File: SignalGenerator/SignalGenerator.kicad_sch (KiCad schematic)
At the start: 36 parts, among them J1 Buss PD, J2 AVR-ICSP, J3 I2C Display, J4 Conn_Coaxial, J5 Screw_Terminal_01x04, J6 Power, SW1 SW_Push_SPDT, U2 ATmega328-A, U5 AD8021, U6 AD9833BRMZ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

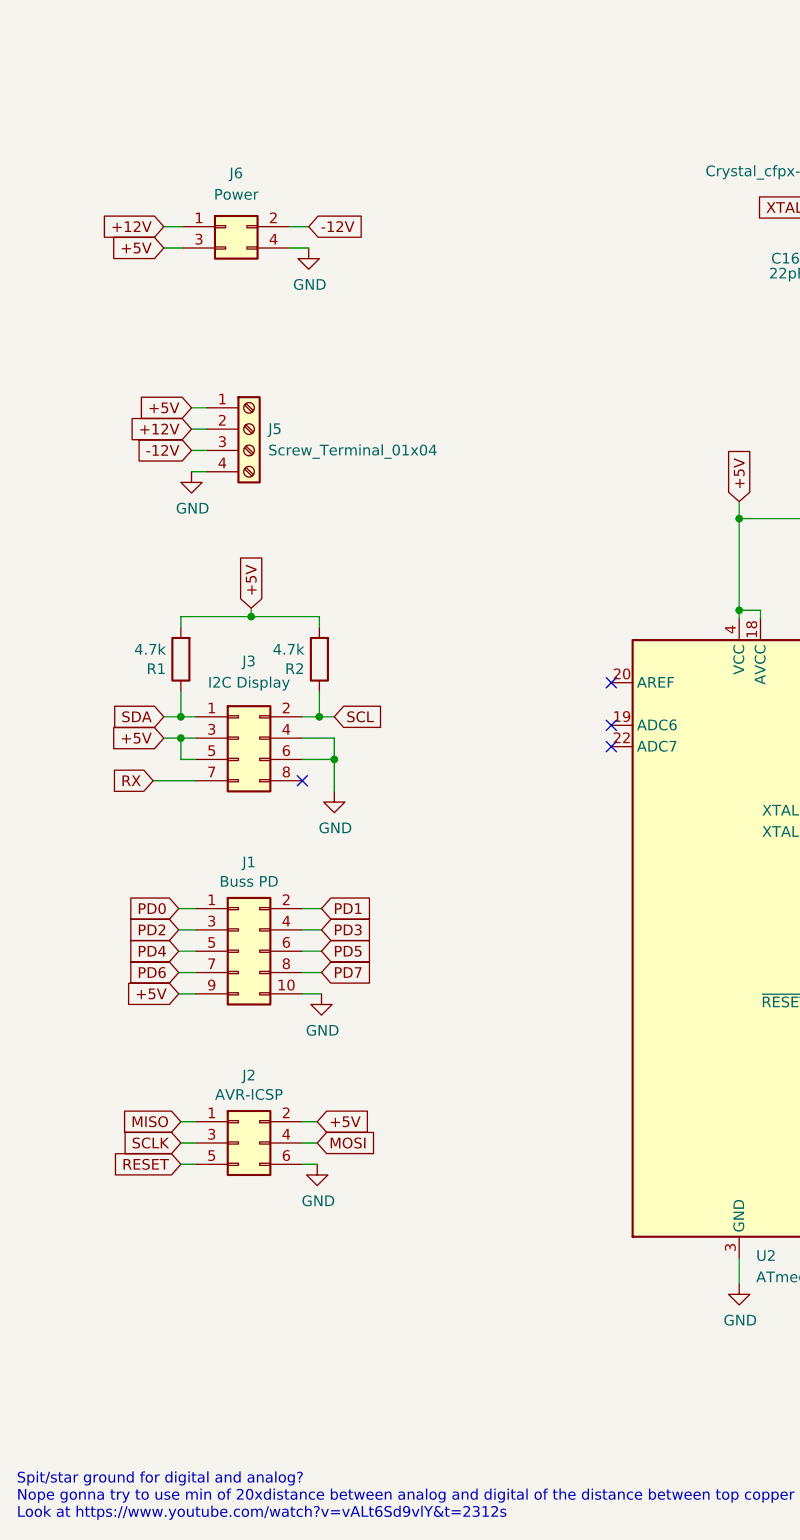
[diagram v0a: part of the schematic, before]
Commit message: added rotary encoder stuff
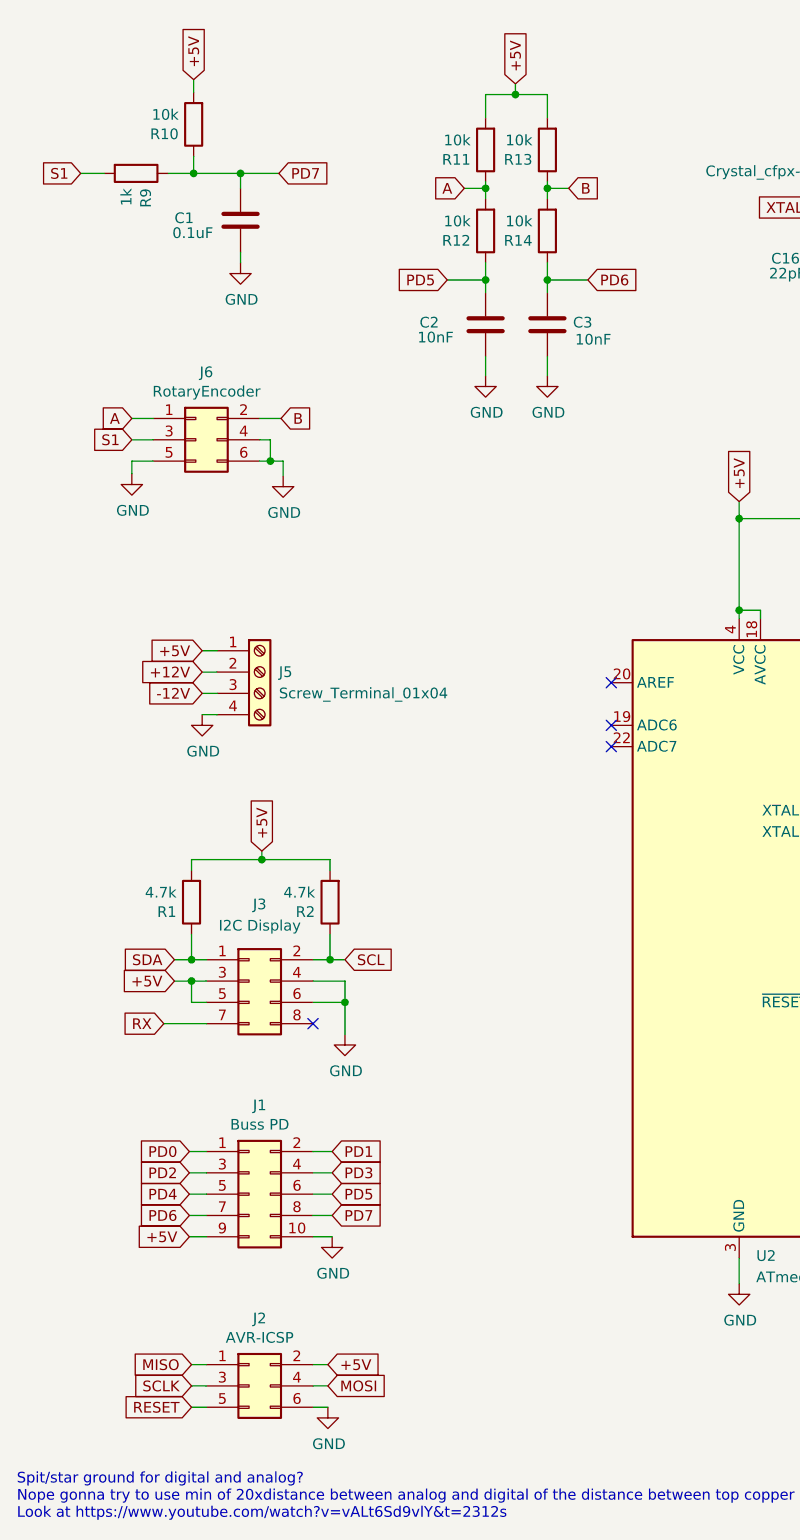
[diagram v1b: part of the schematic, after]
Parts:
- removed J6: Power, Connector_PinHeader_2.54mm:PinHeader_2x02_P2.54mm_Vertical, symbol Connector_Generic:Conn_02x02_Odd_Even
- added C1: 0.1uF, Capacitor_SMD:C_0805_2012Metric_Pad1.18x1.45mm_HandSolder, symbol Device:C
- added C2, C3: 10nF, Capacitor_SMD:C_1206_3216Metric_Pad1.33x1.80mm_HandSolder, symbol Device:C
- added J6: RotaryEncoder, Connector_PinHeader_2.54mm:PinHeader_2x03_P2.54mm_Vertical, symbol Connector_Generic:Conn_02x03_Odd_Even
- added R10, R11, R12, R13, R14: 10k, Resistor_SMD:R_0805_2012Metric_Pad1.20x1.40mm_HandSolder, symbol Device:R
- added R9: 1k, Resistor_SMD:R_0805_2012Metric_Pad1.20x1.40mm_HandSolder, symbol Device:R
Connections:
- net +5V: now also R10.2, R11.2, R13.2
- net GND: now also C1.2, C2.2, C3.2, J6.4 (Pin_4), J6.5 (Pin_5), J6.6 (Pin_6)
- net PD5: now also C2.1, R12.1
- net PD6: now also C3.1, R14.1
- net PD7: now also C1.1, R10.1, R9.1
- new net A: J6.1 (Pin_1), R11.1, R12.2
- new net B: J6.2 (Pin_2), R13.1, R14.2
- new net S1: J6.3 (Pin_3), R9.2
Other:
- moved on the sheet: J1, J2, J3, J5, R1, R2
